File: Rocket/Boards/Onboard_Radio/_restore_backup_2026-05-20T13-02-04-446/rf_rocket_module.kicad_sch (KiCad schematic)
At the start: 13 parts

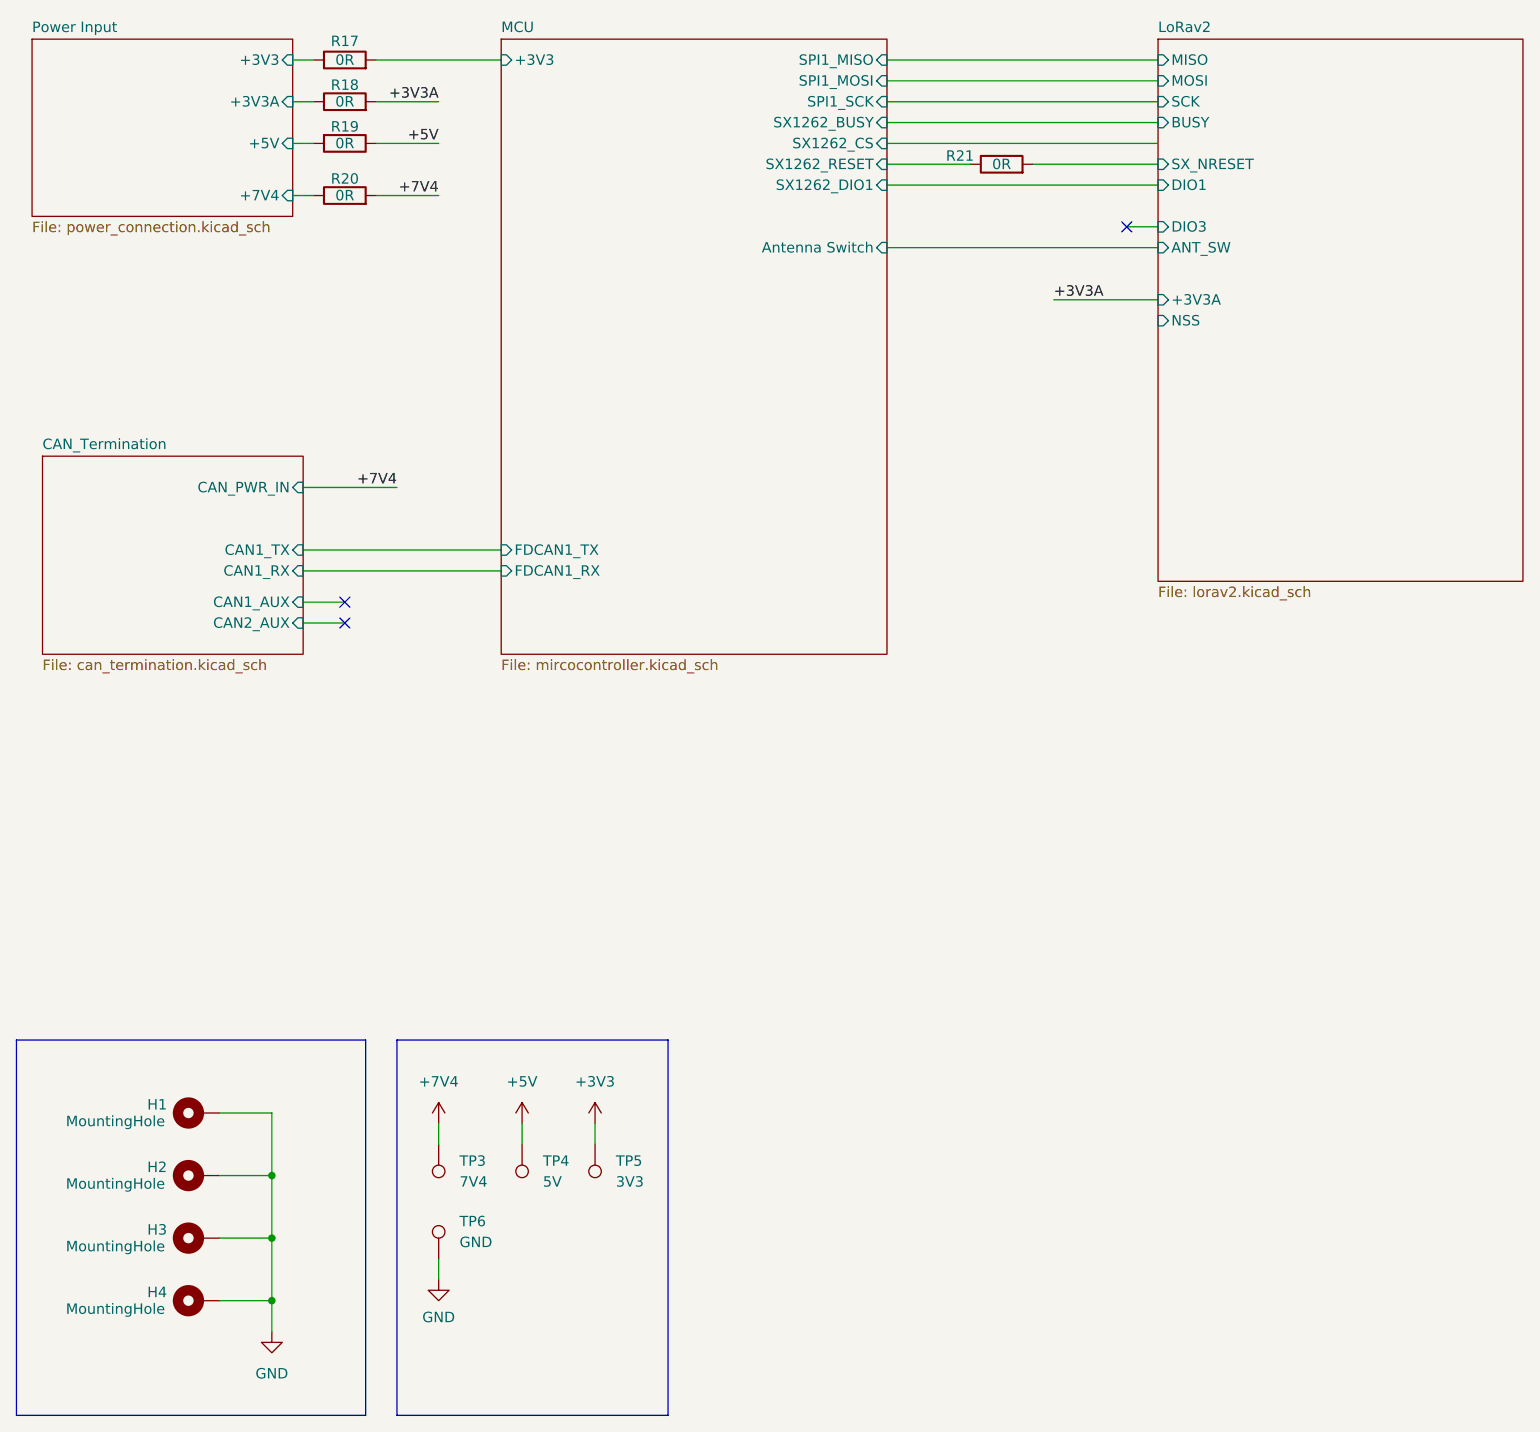
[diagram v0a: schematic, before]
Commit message: schematic bom needs updating and traces need finishing
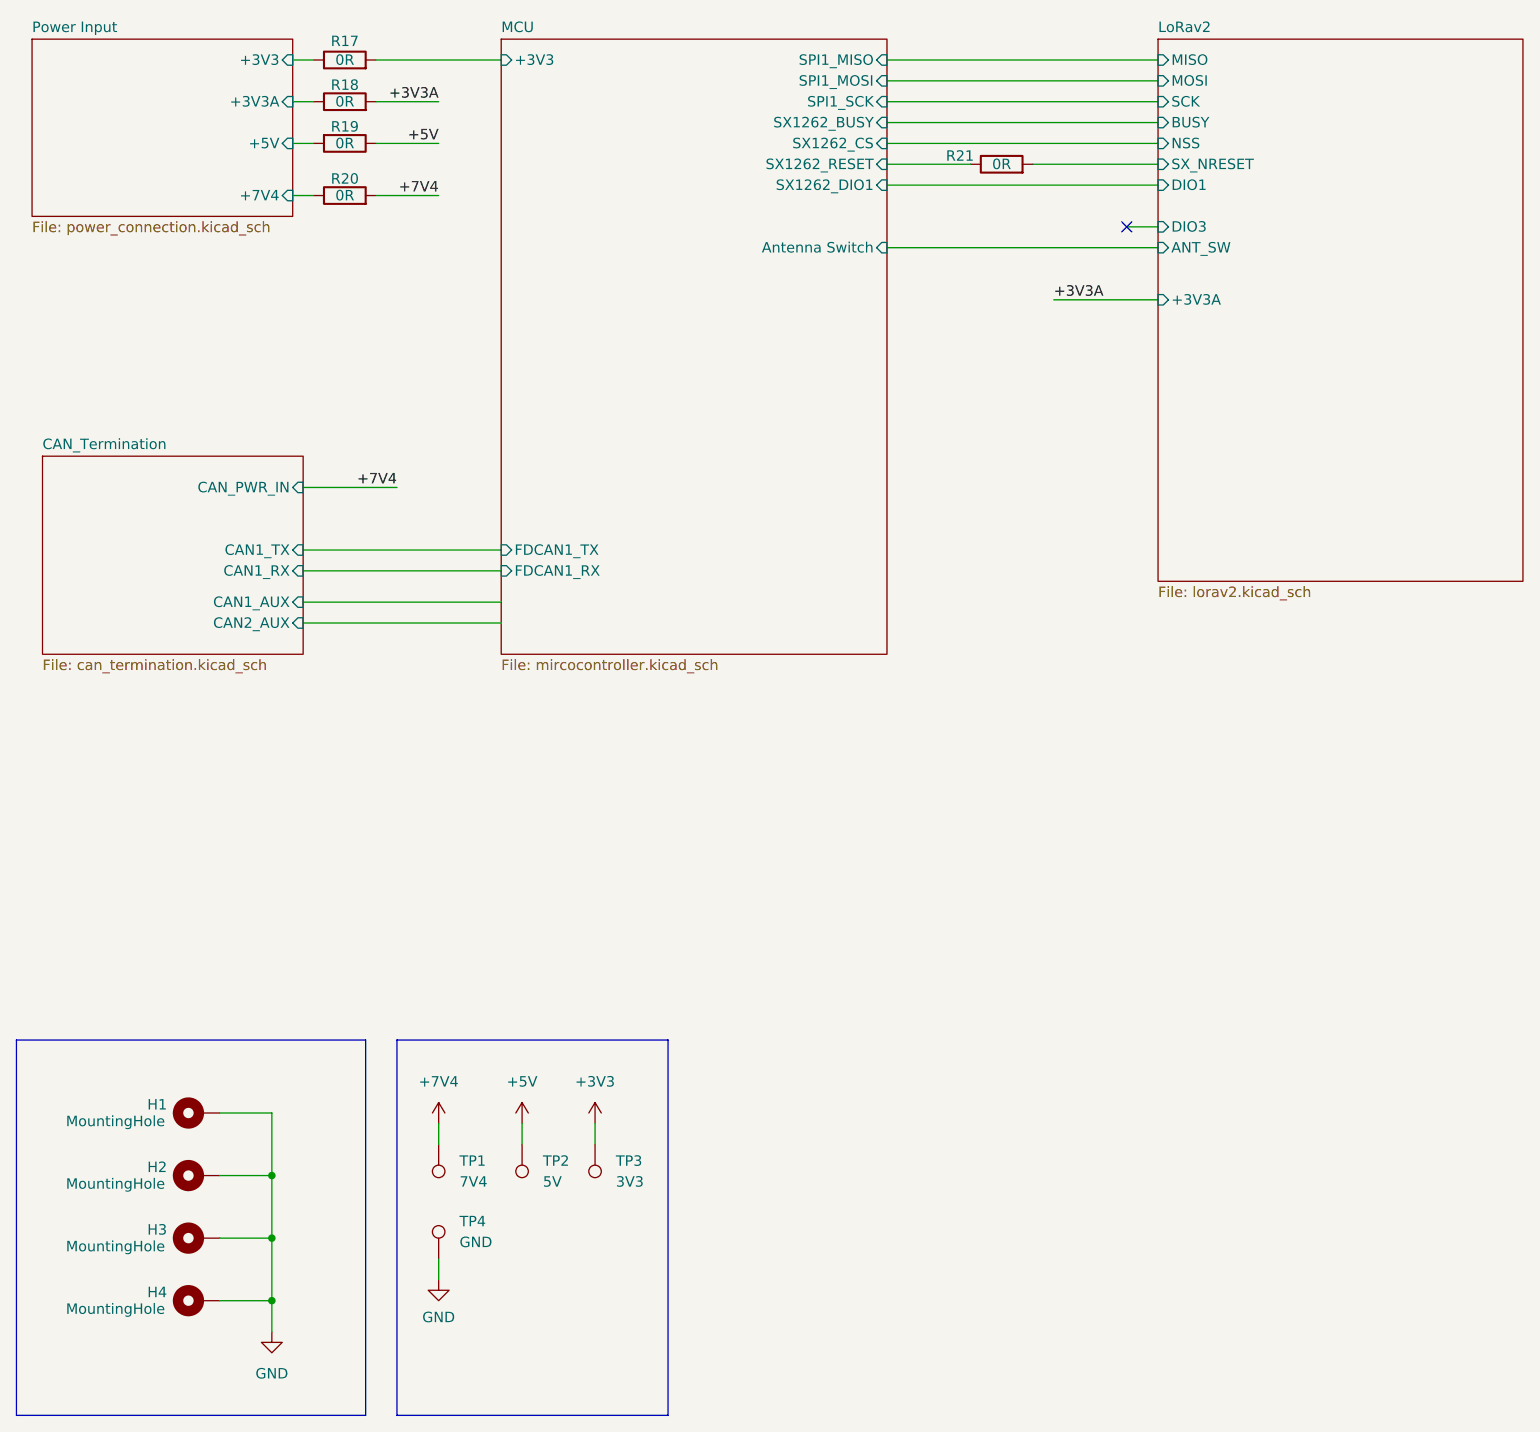
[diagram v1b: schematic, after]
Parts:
- renumbered TP3 to TP1, TP4 to TP2, TP5 to TP3, TP6 to TP4
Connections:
- no-connect marks 3 -> 1
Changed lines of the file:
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@@
-	)
-	(no_connect
-		(at 58.42 88.9)
 	)
 	(no_connect
 		(at 153.67 43.18)
 	)
-	(no_connect
-		(at 58.42 91.44)
+	(wire
+		(pts
+			(xy 53.34 88.9) (xy 77.47 88.9)
+		)
+		(stroke
+			(width 0)
+			(type default)
+		)
 	)
 	(wire
@@
 	(wire
 		(pts
-			(xy 53.34 88.9) (xy 58.42 88.9)
-		)
-		(stroke
-			(width 0)
-			(type default)
-		)
-	)
-	(wire
-		(pts
 			(xy 69.85 152.4) (xy 69.85 154.94)
 		)
@@
 	(wire
 		(pts
-			(xy 53.34 91.44) (xy 58.42 91.44)
+			(xy 53.34 91.44) (xy 77.47 91.44)
 		)
 		(stroke
@@
 		(dnp no)
 		(fields_autoplaced yes)
-		(property "Reference" "TP4"
+		(property "Reference" "TP2"
 			(at 82.55 156.9719 0)
 			(show_name no)
@@
 			(project "rf_rocket_module"
 				(path "/4940ffbe-f45f-4917-a247-12e2b32b6c35"
-					(reference "TP4")
+					(reference "TP2")
 					(unit 1)
 				)
@@
 		(exclude_from_sim no)
 		(in_bom no)
-		(on_board no)
+		(on_board yes)
 		(in_pos_files yes)
 		(dnp no)
@@
 		(dnp no)
 		(fields_autoplaced yes)
-		(property "Reference" "TP5"
+		(property "Reference" "TP3"
 			(at 91.44 156.9719 0)
 			(show_name no)
@@
 			(project "rf_rocket_module"
 				(path "/4940ffbe-f45f-4917-a247-12e2b32b6c35"
-					(reference "TP5")
+					(reference "TP3")
 					(unit 1)
 				)
@@
 		(exclude_from_sim no)
 		(in_bom no)
-		(on_board no)
+		(on_board yes)
 		(in_pos_files yes)
 		(dnp no)
@@
 		(exclude_from_sim no)
 		(in_bom no)
-		(on_board no)
+		(on_board yes)
 		(in_pos_files yes)
 		(dnp no)
@@
 		(dnp no)
 		(fields_autoplaced yes)
-		(property "Reference" "TP3"
+		(property "Reference" "TP1"
 			(at 72.39 156.9719 0)
 			(show_name no)
@@
 			(project "rf_rocket_module"
 				(path "/4940ffbe-f45f-4917-a247-12e2b32b6c35"
-					(reference "TP3")
+					(reference "TP1")
 					(unit 1)
 				)
@@
 		(dnp no)
 		(fields_autoplaced yes)
-		(property "Reference" "TP6"
+		(property "Reference" "TP4"
 			(at 72.39 164.3379 0)
 			(show_name no)
@@
 			(project "rf_rocket_module"
 				(path "/4940ffbe-f45f-4917-a247-12e2b32b6c35"
-					(reference "TP6")
+					(reference "TP4")
 					(unit 1)
 				)
@@
 		(exclude_from_sim no)
 		(in_bom no)
-		(on_board no)
+		(on_board yes)
 		(in_pos_files yes)
 		(dnp no)
@@
 			)
 		)
+		(pin "SX_NRESET" input
+			(at 157.48 35.56 180)
+			(effects
+				(font
+					(size 1.27 1.27)
+				)
+				(justify left)
+			)
+		)
 		(pin "DIO3" input
 			(at 157.48 43.18 180)
@@
 			)
 		)
+		(pin "NSS" input
+			(at 157.48 33.02 180)
+			(effects
+				(font
+					(size 1.27 1.27)
+				)
+				(justify left)
+			)
+		)
 		(pin "BUSY" input
 			(at 157.48 30.48 180)
@@
 			(effects
 				(font
-					(size 1.27 1.27)
-				)
-				(justify left)
-			)
-		)
-		(pin "NSS" input
-			(at 157.48 54.61 180)
-			(effects
-				(font
-					(size 1.27 1.27)
-				)
-				(justify left)
-			)
-		)
-		(pin "SX_NRESET" input
-			(at 157.48 35.56 180)
-			(effects
-				(font
